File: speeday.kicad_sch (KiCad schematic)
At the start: 1 part, among them U1 STM32F107V_B-C_Tx

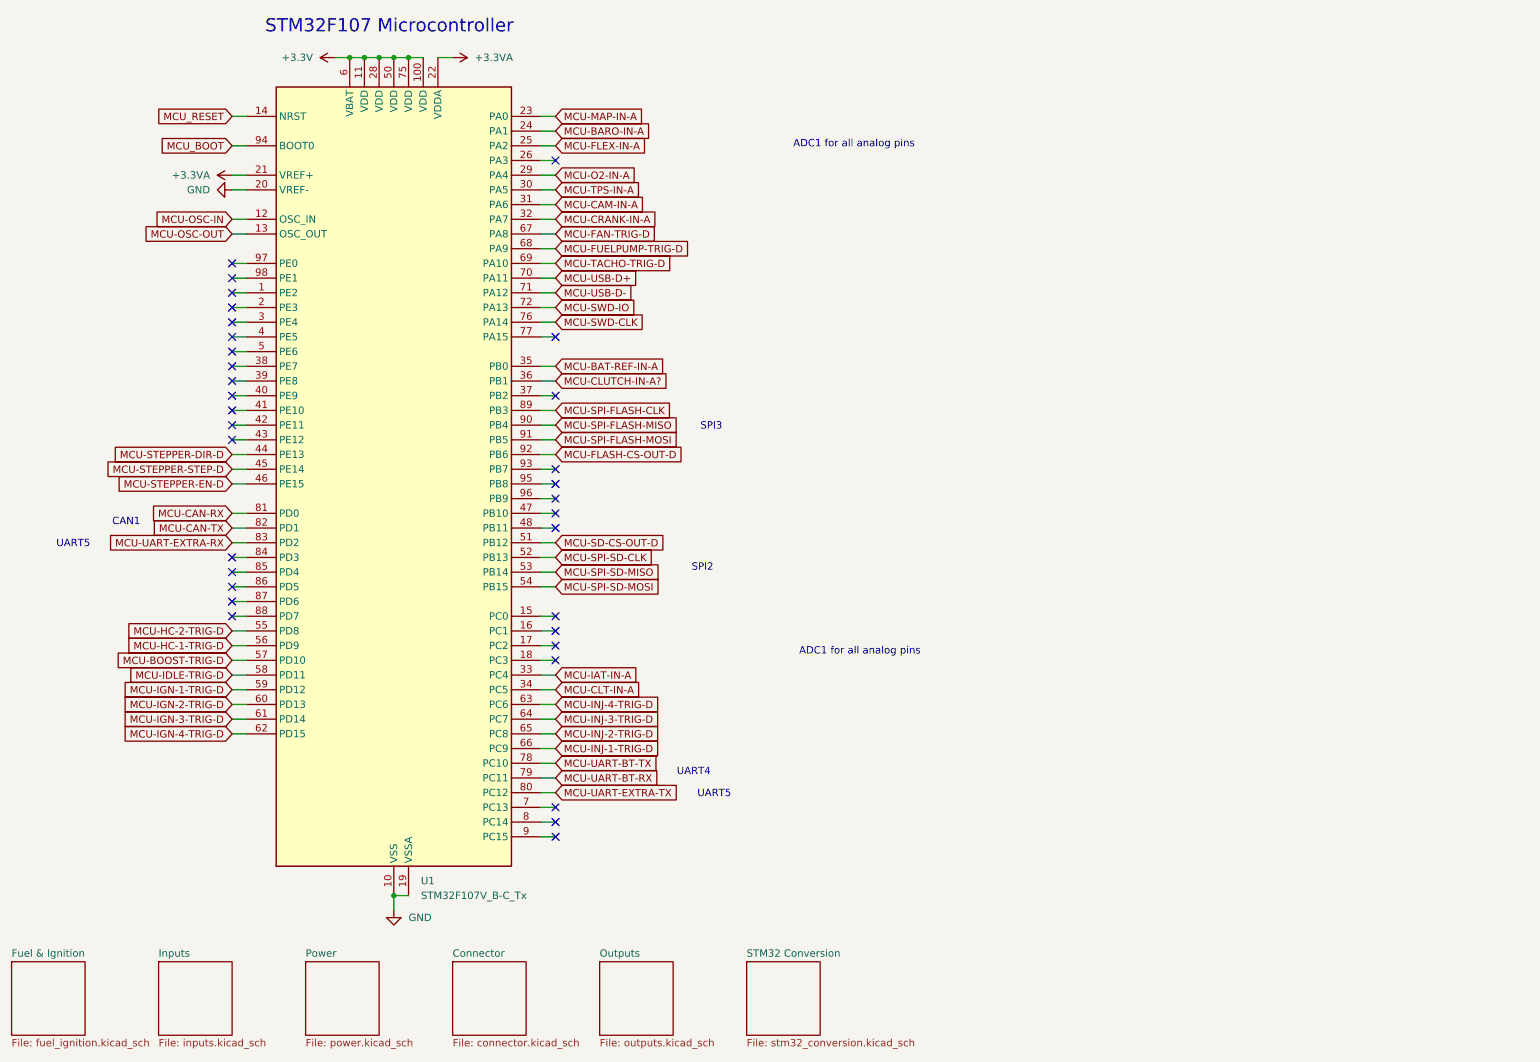
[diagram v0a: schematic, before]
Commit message: Add additional IOs
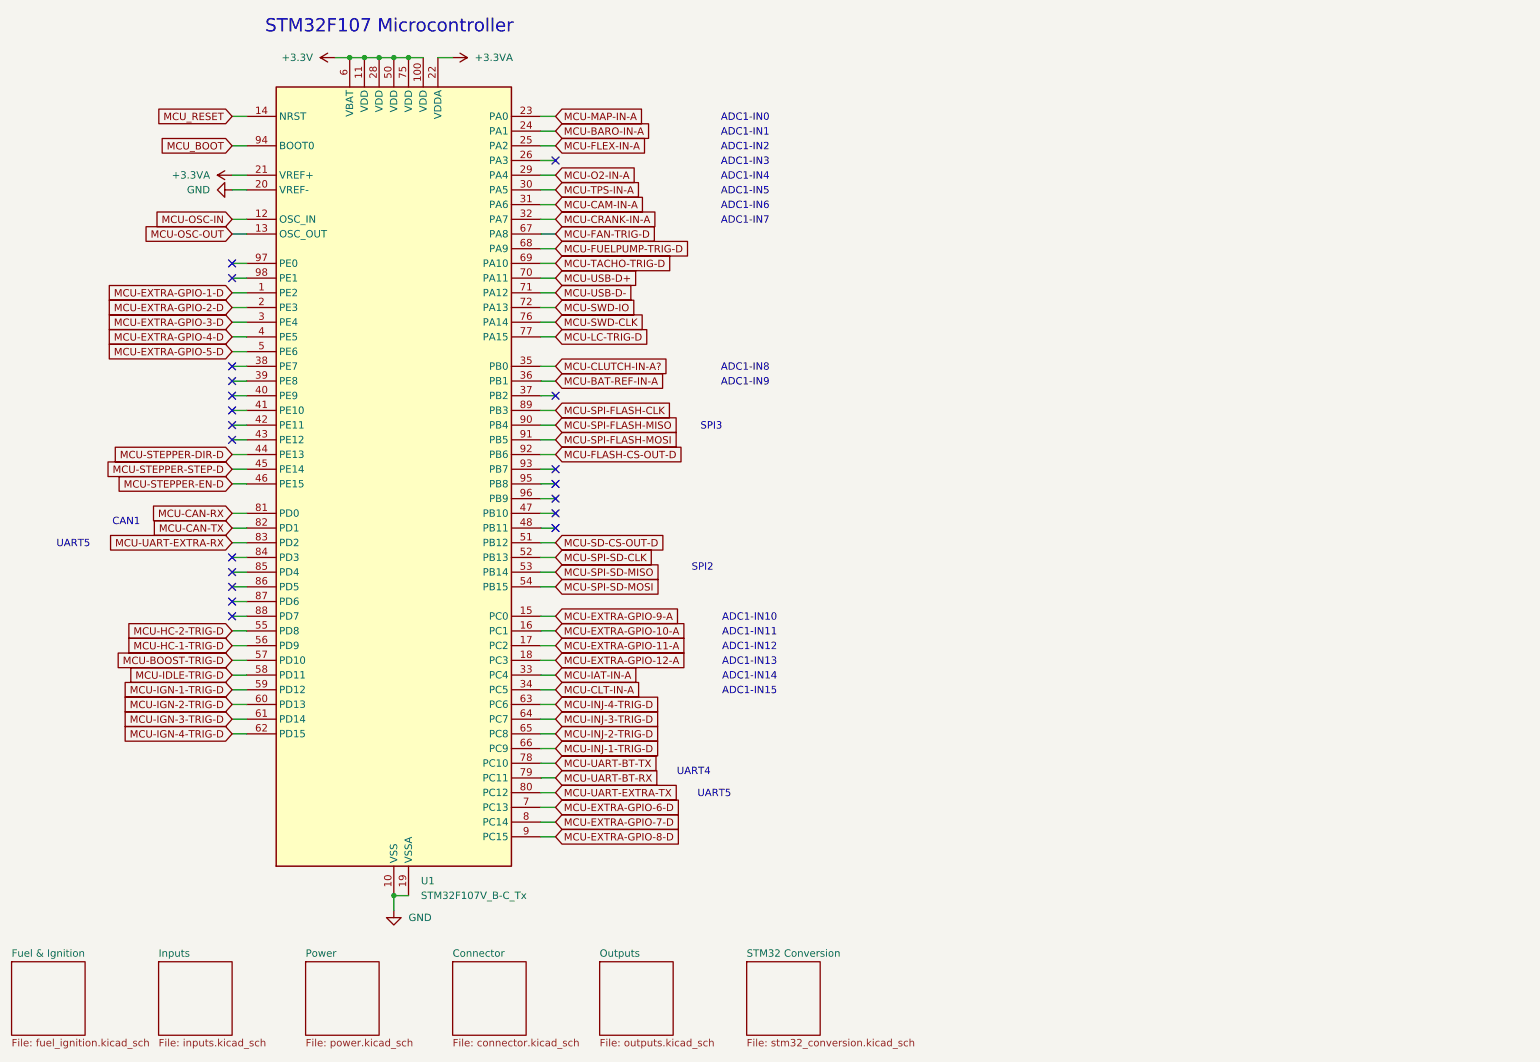
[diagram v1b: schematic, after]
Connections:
- net MCU-BAT-REF-IN-A: now also U1.36 (PB1); no longer U1.35 (PB0)
- net MCU-CLUTCH-IN-A?: now also U1.35 (PB0); no longer U1.36 (PB1)
- net MCU-EXTRA-GPIO-1-D: now reaches U1.1 (PE2)
- net MCU-EXTRA-GPIO-9-A: now reaches U1.15 (PC0)
- net MCU-EXTRA-GPIO-10-A: now reaches U1.16 (PC1)
- net MCU-EXTRA-GPIO-11-A: now reaches U1.17 (PC2)
- net MCU-EXTRA-GPIO-12-A: now reaches U1.18 (PC3)
- net MCU-EXTRA-GPIO-2-D: now reaches U1.2 (PE3)
- net MCU-EXTRA-GPIO-3-D: now reaches U1.3 (PE4)
- net MCU-EXTRA-GPIO-4-D: now reaches U1.4 (PE5)
- net MCU-EXTRA-GPIO-5-D: now reaches U1.5 (PE6)
- net MCU-EXTRA-GPIO-6-D: now reaches U1.7 (PC13)
- net MCU-LC-TRIG-D: now reaches U1.77 (PA15)
- net MCU-EXTRA-GPIO-7-D: now reaches U1.8 (PC14)
- net MCU-EXTRA-GPIO-8-D: now reaches U1.9 (PC15)
- no-connect marks 33 -> 20
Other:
- note added: "ADC1-IN0"
- note added: "ADC1-IN1"
- note added: "ADC1-IN10"
- note added: "ADC1-IN11"
- note added: "ADC1-IN12"
- note added: "ADC1-IN13"
- note added: "ADC1-IN14"
- note added: "ADC1-IN15"
- note added: "ADC1-IN2"
- note added: "ADC1-IN3"
- note added: "ADC1-IN4"
- note added: "ADC1-IN5"
- note added: "ADC1-IN6"
- note added: "ADC1-IN7"
- note added: "ADC1-IN8"
- note added: "ADC1-IN9"
- note removed: "ADC1 for all analog pins"

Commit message: Pre MCU switch
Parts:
- added U7: STM32F407VGTx, Package_QFP:LQFP-176_24x24mm_P0.5mm, symbol MCU_ST_STM32F4:STM32F407VGTx
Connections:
- net +3.3V: now also U7.100 (VDD), U7.11 (VDD), U7.19 (VDD), U7.28 (VDD), U7.50 (VDD), U7.6 (VBAT), U7.75 (VDD)
- net +3.3VA: now also U7.21 (VREF+), U7.22 (VDDA)
- net GND: now also U7.10 (VSS), U7.20 (VSSA), U7.27 (VSS), U7.74 (VSS), U7.99 (VSS)
- net MCU-BARO-IN-A: now also U1.35 (PB0), U7.35 (PB0); no longer U1.24 (PA1)
- net MCU-BAT-REF-IN-A: now also U7.36 (PB1)
- net MCU-BOOST-TRIG-D: now also U7.57 (PD10)
- net MCU-CAM-IN-A: now also U1.33 (PC4), U7.33 (PC4); no longer U1.31 (PA6)
- net MCU-CAN-RX: now also U7.81 (PD0)
- net MCU-CAN-TX: now also U7.82 (PD1)
- net MCU-CLT-IN-A: now also U1.31 (PA6), U7.31 (PA6); no longer U1.34 (PC5)
- net MCU-CLUTCH-IN-A?: now also U1.24 (PA1), U7.24 (PA1); no longer U1.35 (PB0)
- net MCU-CRANK-IN-A: now also U7.32 (PA7)
- net MCU-EXTRA-GPIO-1-D: now also U7.1 (PE2)
- net MCU-EXTRA-GPIO-10-A: now also U7.16 (PC1)
- net MCU-EXTRA-GPIO-11-A: now also U7.17 (PC2)
- net MCU-EXTRA-GPIO-12-A: now also U7.18 (PC3)
- net MCU-EXTRA-GPIO-2-D: now also U7.2 (PE3)
- net MCU-EXTRA-GPIO-3-D: now also U7.3 (PE4)
- net MCU-EXTRA-GPIO-4-D: now also U7.4 (PE5)
- net MCU-EXTRA-GPIO-5-D: now also U7.5 (PE6)
- net MCU-EXTRA-GPIO-6-D: now also U7.7 (PC13)
- net MCU-EXTRA-GPIO-7-D: now also U7.8 (PC14)
- net MCU-EXTRA-GPIO-8-D: now also U7.9 (PC15)
- net MCU-EXTRA-GPIO-9-A: now also U7.15 (PC0)
- net MCU-FAN-TRIG-D: now also U7.67 (PA8)
- net MCU-FLASH-CS-OUT-D: now also U7.92 (PB6)
- net MCU-FLEX-IN-A: now also U1.30 (PA5), U7.30 (PA5); no longer U1.25 (PA2)
- net MCU-FUELPUMP-TRIG-D: now also U7.68 (PA9)
- net MCU-HC-1-TRIG-D: now also U7.56 (PD9)
- net MCU-HC-2-TRIG-D: now also U7.55 (PD8)
- net MCU-IAT-IN-A: now also U1.23 (PA0), U7.23 (PA0); no longer U1.33 (PC4)
- net MCU-IDLE-TRIG-D: now also U7.58 (PD11)
- net MCU-IGN-1-TRIG-D: now also U1.66 (PC9), U7.66 (PC9); no longer U1.59 (PD12)
- net MCU-IGN-2-TRIG-D: now also U1.65 (PC8), U7.65 (PC8); no longer U1.60 (PD13)
- net MCU-IGN-3-TRIG-D: now also U1.64 (PC7), U7.64 (PC7); no longer U1.61 (PD14)
- net MCU-IGN-4-TRIG-D: now also U1.63 (PC6), U7.63 (PC6); no longer U1.62 (PD15)
- net MCU-INJ-1-TRIG-D: now also U1.62 (PD15), U7.62 (PD15); no longer U1.66 (PC9)
- net MCU-INJ-2-TRIG-D: now also U1.61 (PD14), U7.61 (PD14); no longer U1.65 (PC8)
- net MCU-INJ-3-TRIG-D: now also U1.60 (PD13), U7.60 (PD13); no longer U1.64 (PC7)
- net MCU-INJ-4-TRIG-D: now also U1.59 (PD12), U7.59 (PD12); no longer U1.63 (PC6)
- net MCU-LC-TRIG-D: now also U7.77 (PA15)
- net MCU-MAP-IN-A: now also U1.34 (PC5), U7.34 (PC5); no longer U1.23 (PA0)
- net MCU-O2-IN-A: now also U7.29 (PA4)
- net MCU-OSC-IN: now also U7.12 (PH0)
- net MCU-OSC-OUT: now also U7.13 (PH1)
- net MCU-SD-CS-OUT-D: now also U7.51 (PB12)
- net MCU-SPI-FLASH-CLK: now also U7.89 (PB3)
- net MCU-SPI-FLASH-MISO: now also U7.90 (PB4)
- net MCU-SPI-FLASH-MOSI: now also U7.91 (PB5)
- net MCU-SPI-SD-CLK: now also U7.52 (PB13)
- net MCU-SPI-SD-MISO: now also U7.53 (PB14)
- net MCU-SPI-SD-MOSI: now also U7.54 (PB15)
- net MCU-STEPPER-DIR-D: now also U7.44 (PE13)
- net MCU-STEPPER-EN-D: now also U7.46 (PE15)
- net MCU-STEPPER-STEP-D: now also U7.45 (PE14)
- net MCU-SWD-CLK: now also U7.76 (PA14)
- net MCU-SWD-IO: now also U7.72 (PA13)
- net MCU-TACHO-TRIG-D: now also U7.69 (PA10)
- net MCU-TPS-IN-A: now also U1.25 (PA2), U7.25 (PA2); no longer U1.30 (PA5)
- net MCU-UART-BT-RX: now also U7.79 (PC11)
- net MCU-UART-BT-TX: now also U7.78 (PC10)
- net MCU-UART-EXTRA-RX: now also U7.83 (PD2)
- net MCU-UART-EXTRA-TX: now also U7.80 (PC12)
- net MCU-USB-D+: now also U7.70 (PA11)
- net MCU-USB-D-: now also U7.71 (PA12)
- net MCU_BOOT: now also U7.94 (BOOT0)
- net MCU_RESET: now also U7.14 (NRST)
- new net VCAP: U7.49 (VCAP_1), U7.73 (VCAP_2)
- no-connect marks 20 -> 40

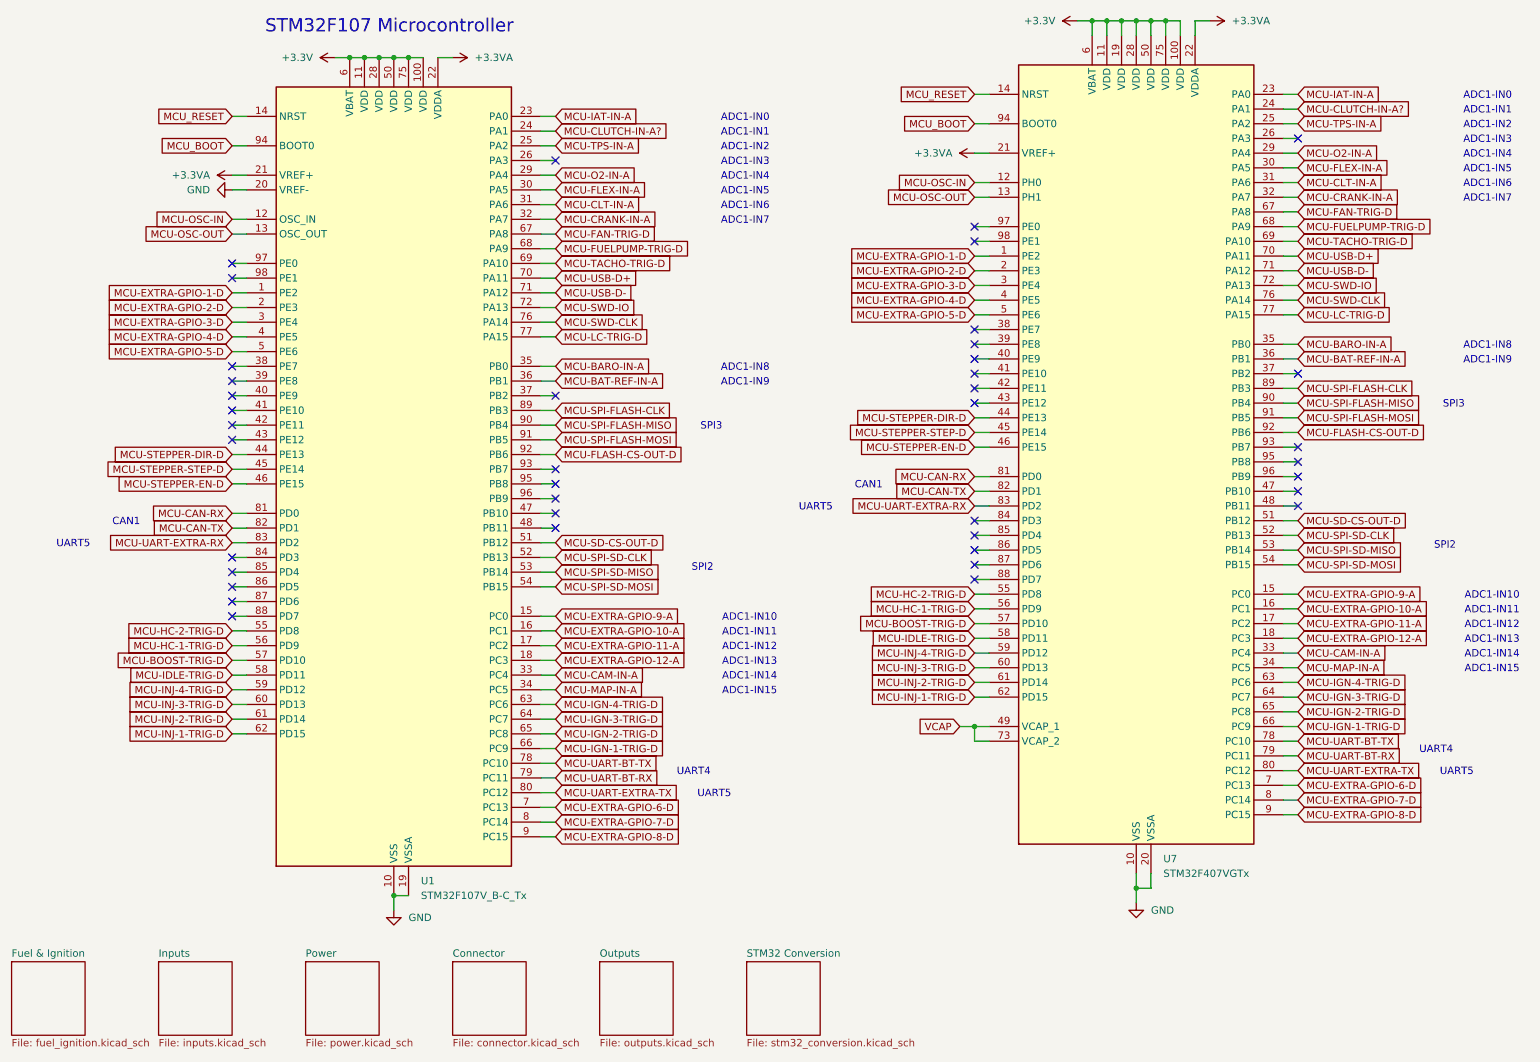
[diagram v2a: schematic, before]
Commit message: Fix MCU decoupling capacitors
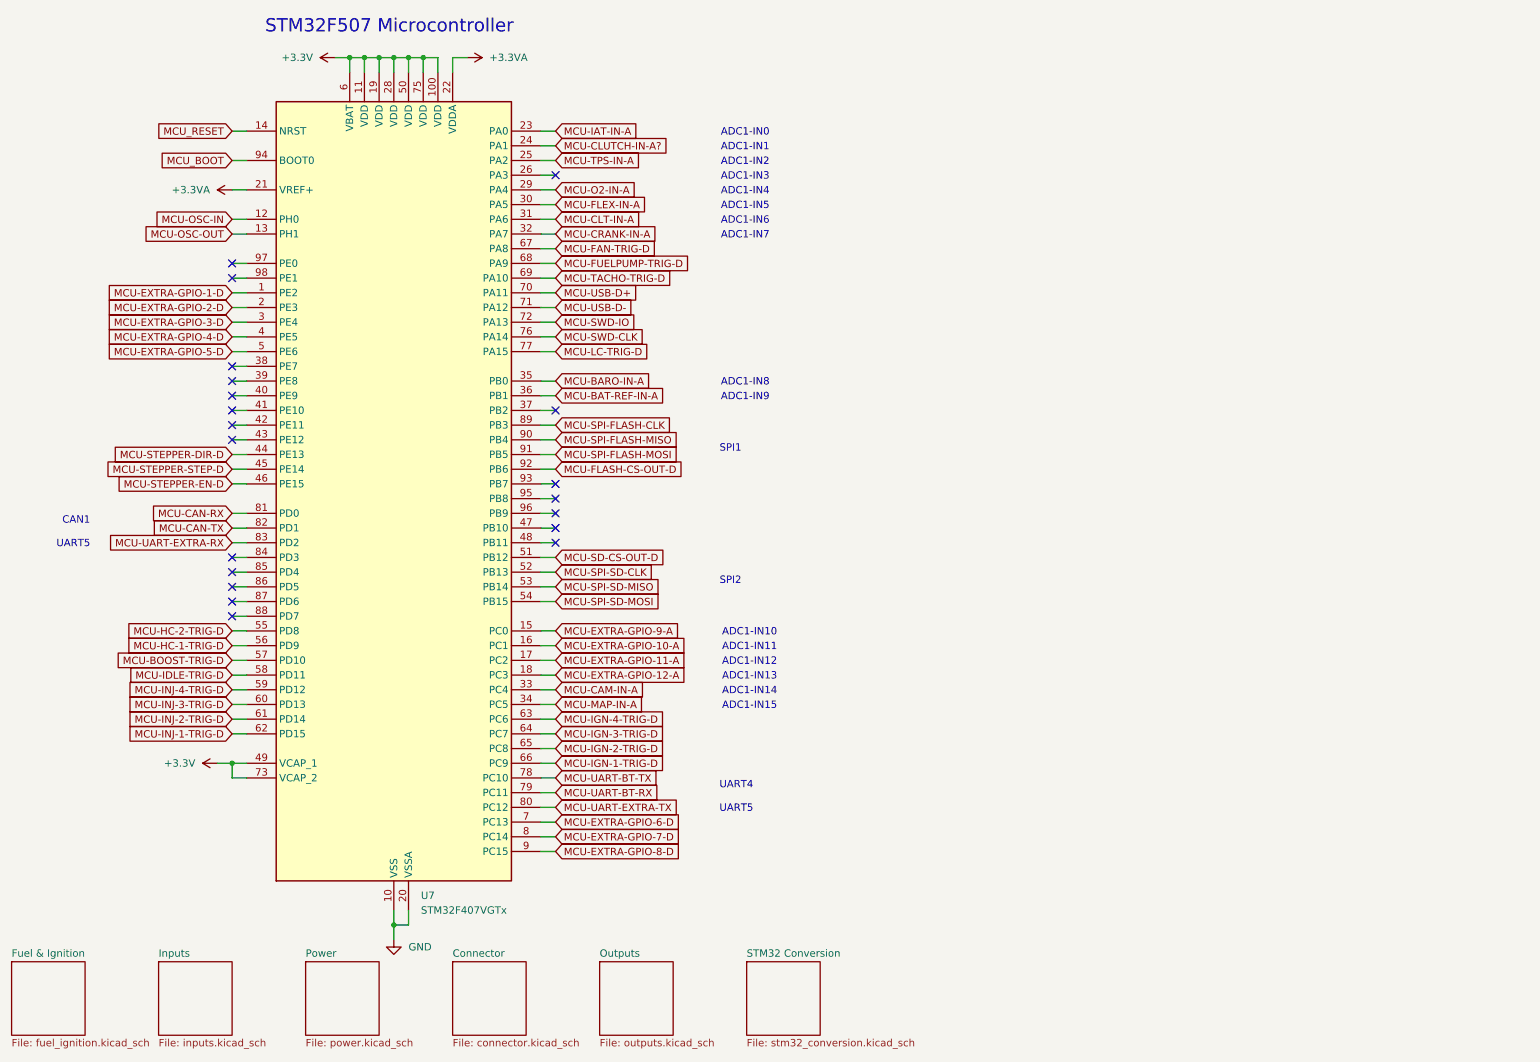
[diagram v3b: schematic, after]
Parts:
- removed U1: STM32F107V_B-C_Tx, Package_QFP:LQFP-100_14x14mm_P0.5mm, symbol MCU_ST_STM32F1:STM32F107V_B-C_Tx
- U7: footprint Package_QFP:LQFP-176_24x24mm_P0.5mm -> Package_QFP:LQFP-100_14x14mm_P0.5mm
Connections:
- net VCAP is gone; now on net +3.3V: U7.49 (VCAP_1), U7.73 (VCAP_2)
- no-connect marks 40 -> 20
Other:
- note added: "SPI1"
- note added: "STM32F507 Microcontroller"
- note removed: "SPI3"
- note removed: "STM32F107 Microcontroller"
- moved on the sheet: U7

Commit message: Fully connect all components
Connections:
- net MCU-CAM-IN-A: now also U7.32 (PA7); no longer U7.33 (PC4)
- net MCU-CLT-IN-A: now also U7.30 (PA5); no longer U7.31 (PA6)
- net MCU-CRANK-IN-A: now also U7.33 (PC4); no longer U7.32 (PA7)
- net MCU-EXTRA-GPIO-10-A: now also U7.15 (PC0); no longer U7.16 (PC1)
- net MCU-EXTRA-GPIO-9-A: now also U7.16 (PC1); no longer U7.15 (PC0)
- net MCU-FAN-TRIG-D: now also U7.69 (PA10); no longer U7.67 (PA8)
- net MCU-FLEX-IN-A: now also U7.23 (PA0); no longer U7.30 (PA5)
- net MCU-IAT-IN-A: now also U7.31 (PA6); no longer U7.23 (PA0)
- net MCU-O2-IN-A: now also U7.25 (PA2); no longer U7.29 (PA4)
- net MCU-TACHO-TRIG-D: now also U7.67 (PA8); no longer U7.69 (PA10)
- net MCU-TPS-IN-A: now also U7.29 (PA4); no longer U7.25 (PA2)
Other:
- sheet Connector renamed Connectors
- sheet STM32 Conversion renamed STM32 Conversion (Analog)
- added sheet STM32 Conversion (Digital/Misc) (stm32_conversion_misc.kicad_sch)
- sheet Connectors: file connector.kicad_sch -> connectors.kicad_sch
- sheet STM32 Conversion (Analog): file stm32_conversion.kicad_sch -> stm32_conversion_analog_digital.kicad_sch
- note added: "STM32F407 Microcontroller"
- note removed: "STM32F507 Microcontroller"
